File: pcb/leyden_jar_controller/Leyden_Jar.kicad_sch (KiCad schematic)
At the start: 90 parts, among them J1 USB_C_Receptacle_USB2.0, J2 Switch matrix connector, J3 SWD/I2C, J4 Ext Port, J7 Breakout, J9 Encoder, SW1 B3U-1000P, SW2 B3U-1000P, SW3 B3U-1000P, SW4 B3U-1000P, U1 W25Q64JVXGIM, U10 MCP4716A0T-E/CH, U2 LMV339, U3 USBLC6-2SC6, U4 TPS7A2033PDBVR, U5 RP2350B, U6 LMV339, U7 TLV74311PDBVR, U8 AP22653W6-7, Y1 ABM8-272-T3

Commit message: [cleanup] V2 schematic: KiCad 10 library symbols and +3V3/+1V1 power symbols.
Co-Authored-By: Claude Opus 5.5 <noreply@anthropic.com>
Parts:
- J1: symbol Connector:USB_C_Receptacle_USB2.0 -> Connector:USB_C_Receptacle_USB2.0_16P
- Y1: footprint rico_footprints:Crystal_SMD_3225-4Pin_3.2x2.5mm -> Leyden_Jar:Crystal_SMD_3225-4Pin_3.2x2.5mm
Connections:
- net GNDPWR: now also J1.SH (SHIELD); no longer J1.S1 (SHIELD)
- net 1V1 renamed +1V1
- net 3V3 renamed +3V3
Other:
- moved on the sheet: R2, R3, U1

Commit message: [cleanup] V2 schematic: everything on the 1.27 mm grid, vertical power symbols.
Co-Authored-By: Claude Opus 5.5 <noreply@anthropic.com>
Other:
- moved on the sheet: C14, C15, C19, C21, FB1, J1, R12, R13, R17, R19, R25, R27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

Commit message: [cleanup] V2 schematic: title block V2 rev 1, J3/J4/JP1 drawing fixes.
Co-Authored-By: Claude Opus 5.5 <noreply@anthropic.com>
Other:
- title: Leyden Jar controller PCB -> Leyden Jar controller PCB V2
- moved on the sheet: J3, J4, R50

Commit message: [cleanup] V2 schematic: block frames and layout rework, comparator fields point to TI LMV339IPWR.
Co-Authored-By: Claude Opus 5.5 <noreply@anthropic.com>
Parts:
- U2, U6: Manufacturer ID LMV339 -> LMV339IPWR; Mouser 863-LMV339DTBR2G -> 595-LMV339IPWR
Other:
- note added: "Breakout header (expansion, split link, ST7789 TFT)"
- note added: "Rotary encoder header"
- note added: "TFT VCC by solder jumper"
- note removed: "Breakout header (expansion, split link, ST7789 TFT), TFT VCC by solder jumper"
- moved on the sheet: C10, C11, C12, C13, C16, C17, C2, C22, C23, C24, C25, C26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

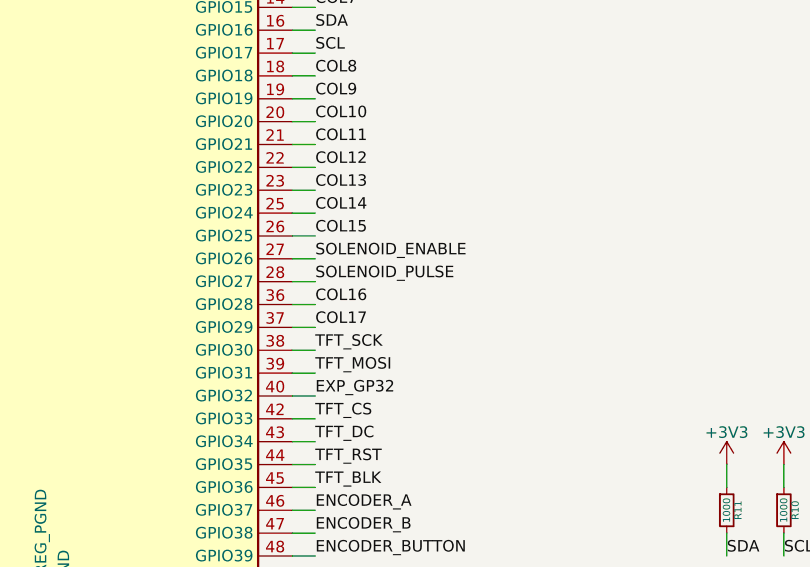
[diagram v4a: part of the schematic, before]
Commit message: [feature] V2: COL16/17 back on GP26/27, U5 rotated 90 degrees so the columns face J2.
Co-Authored-By: Claude Opus 5.5 <noreply@anthropic.com>
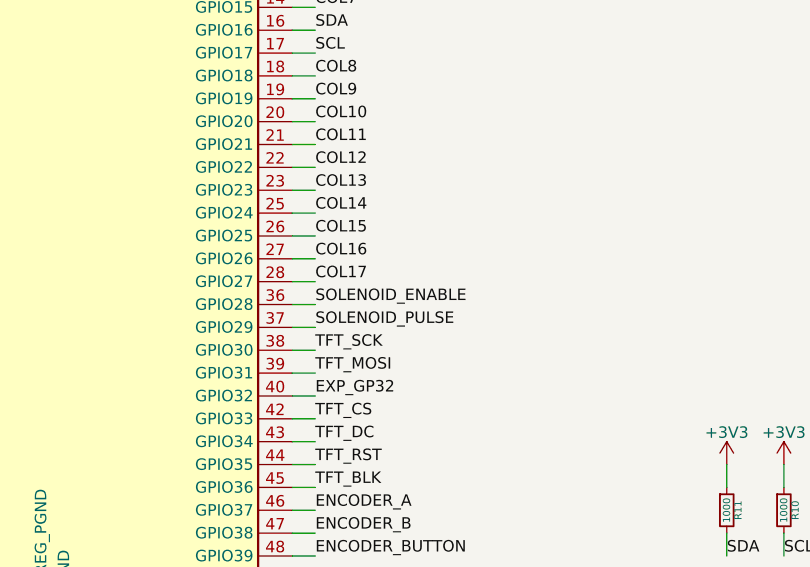
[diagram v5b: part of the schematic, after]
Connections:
- net COL16: now also U5.27 (GPIO26); no longer U5.36 (GPIO28)
- net COL17: now also U5.28 (GPIO27); no longer U5.37 (GPIO29)
- net SOLENOID_ENABLE: now also U5.36 (GPIO28); no longer U5.27 (GPIO26)
- net SOLENOID_PULSE: now also U5.37 (GPIO29); no longer U5.28 (GPIO27)

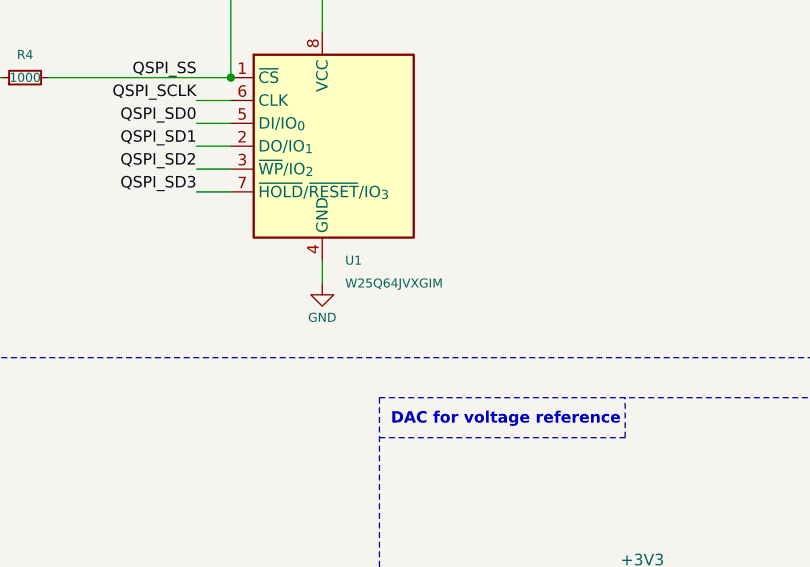
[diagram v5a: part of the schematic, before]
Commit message: [feature] V2: flash U1 changed to the SOIC-8 208 mil W25Q64JVSSIM, nearby parts moved to fit.
Co-Authored-By: Claude Opus 5.5 <noreply@anthropic.com>
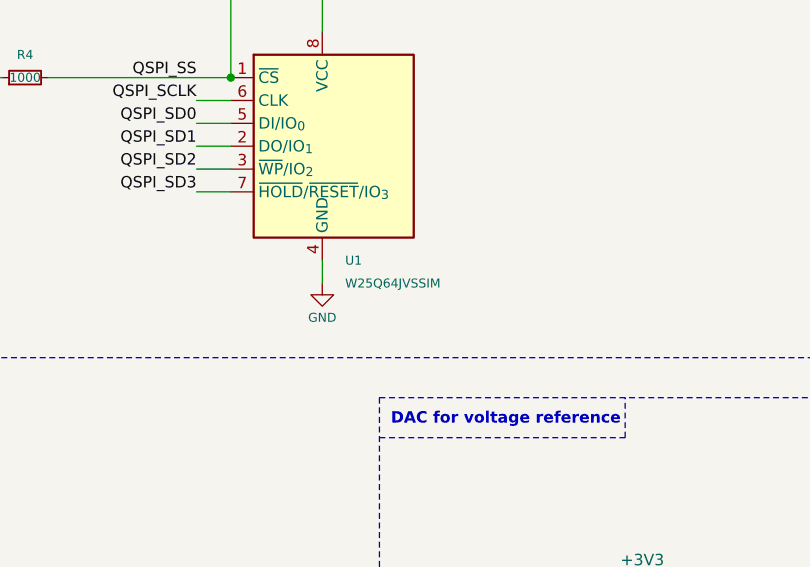
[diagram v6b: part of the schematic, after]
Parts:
- U1: value W25Q64JVXGIM -> W25Q64JVSSIM; footprint Package_SON:WSON-8-1EP_4x4mm_P0.8mm_EP2.2x3mm -> Package_SO:SOIC-8_5.3x5.3mm_P1.27mm; LCSC C6604688 -> C5362615
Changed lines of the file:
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@@
 			)
 		)
-		(property "Value" "W25Q64JVXGIM"
+		(property "Value" "W25Q64JVSSIM"
 			(at 107.95 182.88 0)
 			(show_name no)
@@
 			)
 		)
-		(property "Footprint" "Package_SON:WSON-8-1EP_4x4mm_P0.8mm_EP2.2x3mm"
+		(property "Footprint" "Package_SO:SOIC-8_5.3x5.3mm_P1.27mm"
 			(at 105.41 167.64 0)
 			(hide yes)
@@
 			)
 		)
-		(property "Datasheet" "https://www.mouser.fr/datasheet/2/949/w25q16jv_spi_revg_03222018_plus-1489727.pdf"
+		(property "Datasheet" "https://www.lcsc.com/datasheet/C5362615.pdf"
 			(at 105.41 167.64 0)
 			(hide yes)
@@
 			)
 		)
-		(property "LCSC" "C6604688"
+		(property "LCSC" "C5362615"
 			(at 105.41 167.64 0)
 			(hide yes)
